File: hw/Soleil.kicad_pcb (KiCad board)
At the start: 2 copper layers, 31.4 x 44 mm, 41 parts, among them J1 Conn_01x04, Q1 Si2301, Q2 2N7002, SW1 SW_Push, U1 SPV1040TTR, U2 SPX3819M5-L-3-3, U3 STM32G030F6Px, U4 ZJY200200-0154DAAMFGN

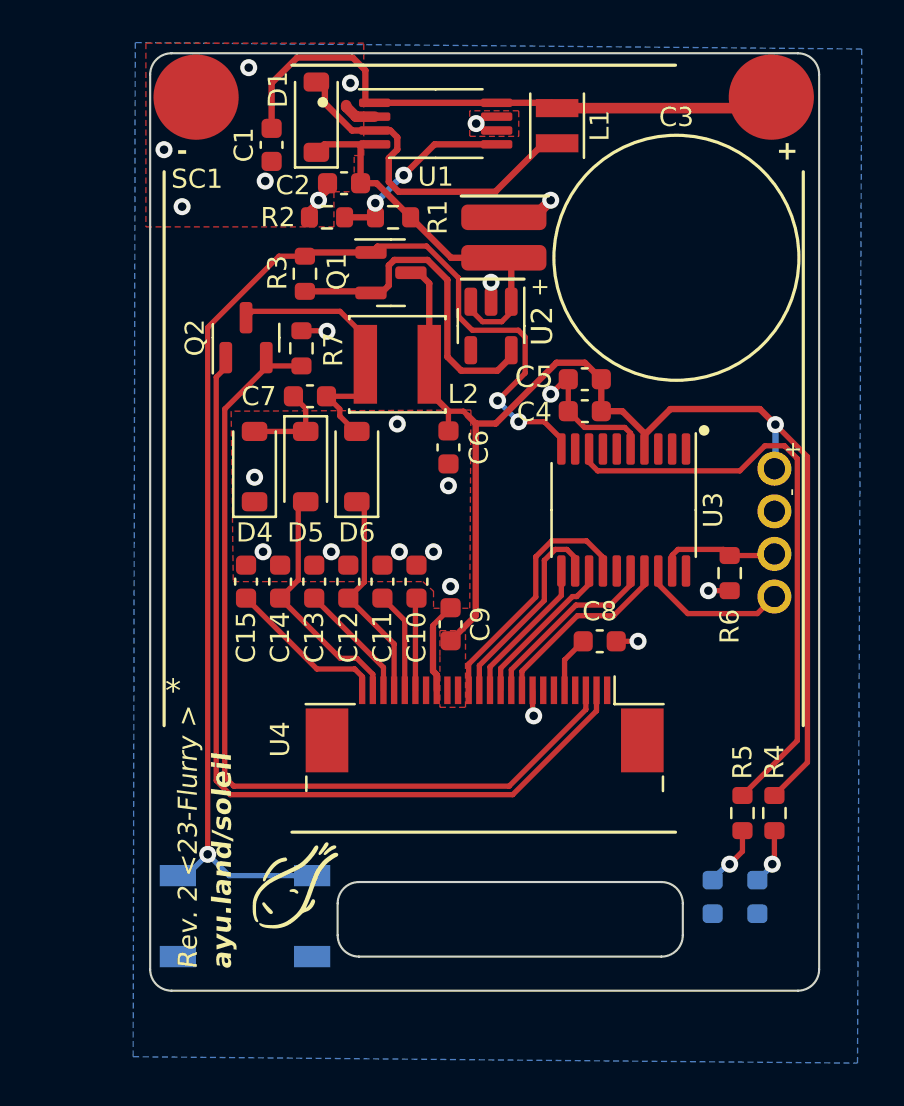
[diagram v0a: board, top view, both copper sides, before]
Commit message: (WIP) Update PCB layout, routing to-do
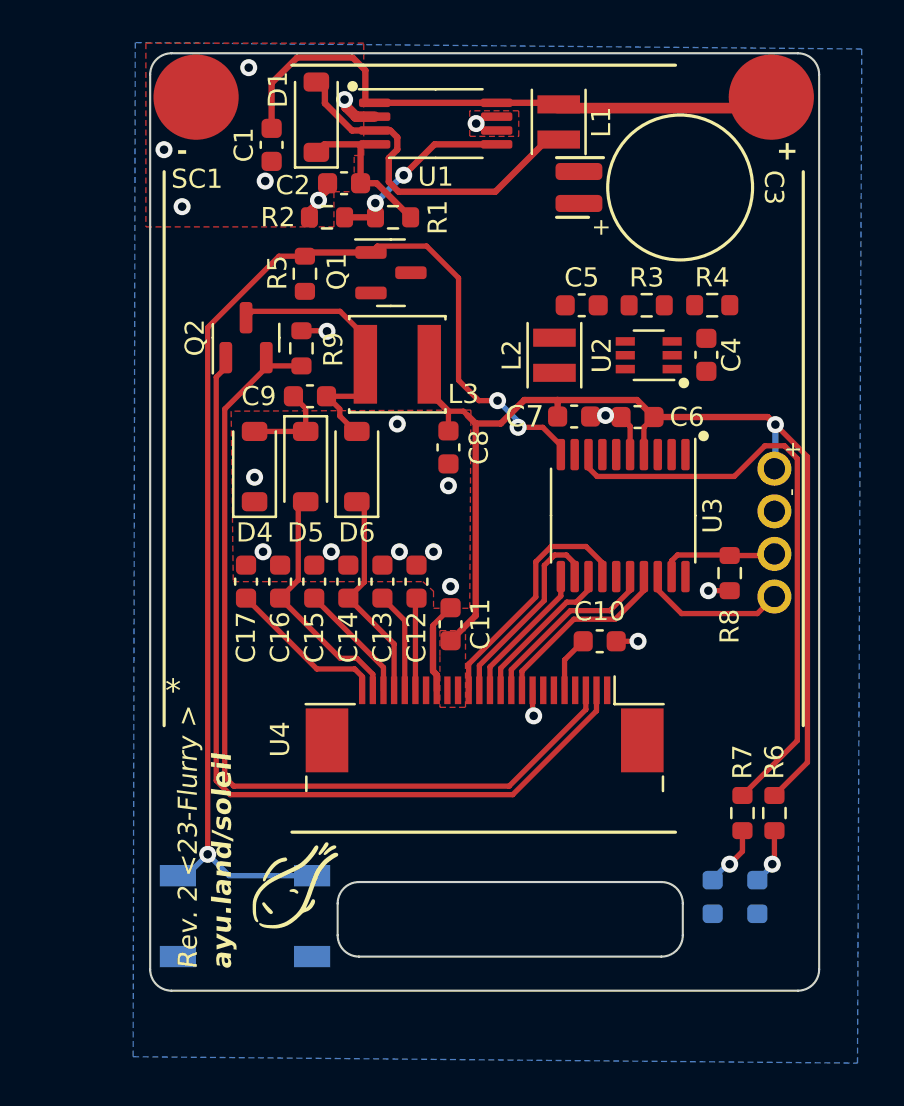
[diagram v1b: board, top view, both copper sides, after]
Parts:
- added C4: 10u, Capacitor_SMD:C_0603_1608Metric, F.Cu at (32.2, 23.6)
- added C5: 10u, Capacitor_SMD:C_0603_1608Metric, F.Cu at (26.4, 21.2)
- added L2: 10u, Inductor_SMD:L_Sunlord_SWPA252012S, F.Cu at (25.1, 23.6)
- added R3: 560k, Resistor_SMD:R_0603_1608Metric, F.Cu at (29.4, 21.2)
- added R4: 100k, Resistor_SMD:R_0603_1608Metric, F.Cu at (32.5, 21.2)
- C3: value 470m -> 220m; footprint Soleil_footprints:SuperCap_D11.5 -> Soleil_footprints:DMS3R3
- R1: value 750k -> 360k
- R7: renamed from R5; value 1k -> 820
- U2: value SPX3819M5-L-3-3 -> TPS61220DCK; footprint Package_TO_SOT_SMD:SOT-23-5 -> Package_TO_SOT_SMD:Texas_R-PDSO-G6
- moved U2 7.53 mm to (29.5, 23.6), turned to 180 degrees
- moved C3 3.30 mm to (31.0, 15.7)
- moved C6 2.49 mm to (29.0, 26.5)
- moved C7 1.82 mm to (26.0, 26.4), turned to 180 degrees
- moved U3 0.26 mm to (28.3, 31.1)
- moved L1 0.19 mm to (25.3, 12.6)
- renumbered C8 to C10, C9 to C11, C10 to C12, C11 to C13, C12 to C14, C13 to C15, C14 to C16, C15 to C17, C4 to C6, C5 to C7, C6 to C8, C7 to C9, L2 to L3, R3 to R5, R4 to R6, R6 to R8, R7 to R9
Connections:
- C2 pad 1: Net-(D1-K) -> VCAP
- C3 pad 1: Net-(D1-K) -> VCAP
- D1 pad 1: Net-(D1-K) -> VCAP
- Q1 pad 2: VREF -> VCAP
- Q1 pad 3: VDD -> VREF
- R1 pad 1: Net-(D1-K) -> VCAP
- R5 pad 1: VREF -> VCAP
- U1 pad 4: Net-(D1-K) -> VCAP
- U2 pad 1: Net-(D1-K) -> VREF
- U2 pad 2: GND -> Net-(U2-FB)
- U2 pad 3: Net-(D1-K) -> GND
- U2 pad 4: unconnected-(U2-BP-Pad4) -> VDD
- U2 pad 5: VREF -> Net-(U2-L)
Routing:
- net Net-(D1-K): track 18.3 -> 0.00 mm
- net VREF: track 15.8 -> 0.00 mm
- net VCAP: track 0.00 -> 7.71 mm
- net GND: track 20.8 -> 14.3 mm, vias 22 -> 20
- net VDD: track 61.0 -> 54.9 mm
- net PWR_LATCH: track 58.9 -> 57.1 mm

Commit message: Finish routing for the updated board
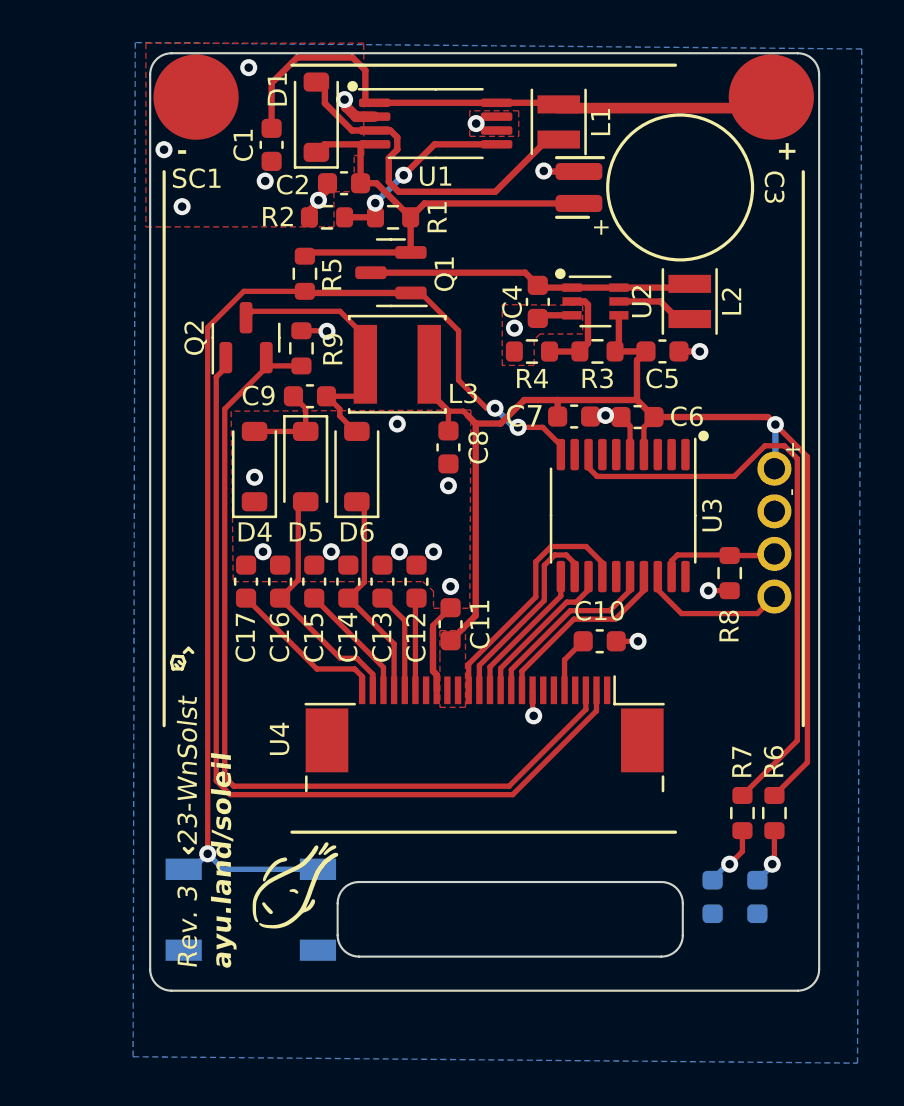
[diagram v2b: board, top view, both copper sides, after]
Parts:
- moved R4 8.74 mm to (24.0, 23.4), turned to 180 degrees
- moved C4 8.29 mm to (24.3, 21.1), turned to -90 degrees
- moved L2 6.83 mm to (31.4, 21.1), turned to -90 degrees
- moved C5 4.36 mm to (30.1, 23.4), turned to 0 degrees
- moved U2 3.55 mm to (27.0, 21.1), turned to 0 degrees
- moved R3 3.17 mm to (27.1, 23.4), turned to 180 degrees
- moved SW1 0.41 mm to (10.8, 49.6)
- turned Q1 to 180 degrees
- turned R5 to -90 degrees
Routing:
- net VREF: track 0.00 -> 15.3 mm
- net VCAP: track 7.71 -> 22.6 mm
- net VDD: track 54.9 -> 60.5 mm
- net Net-(U2-FB): track 0.00 -> 4.59 mm
- net GND: track 14.3 -> 18.6 mm, vias 20 -> 23
- net Net-(U2-L): track 0.00 -> 3.67 mm
- net PWR_LATCH: track 57.1 -> 53.7 mm
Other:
- board text added: "23-WnSolst"
- board text added: "Rev. 3"
- board text removed: "*"
- board text removed: "Rev. 2 <23-Flurry >"

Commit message: Add capacitor voltage sensing
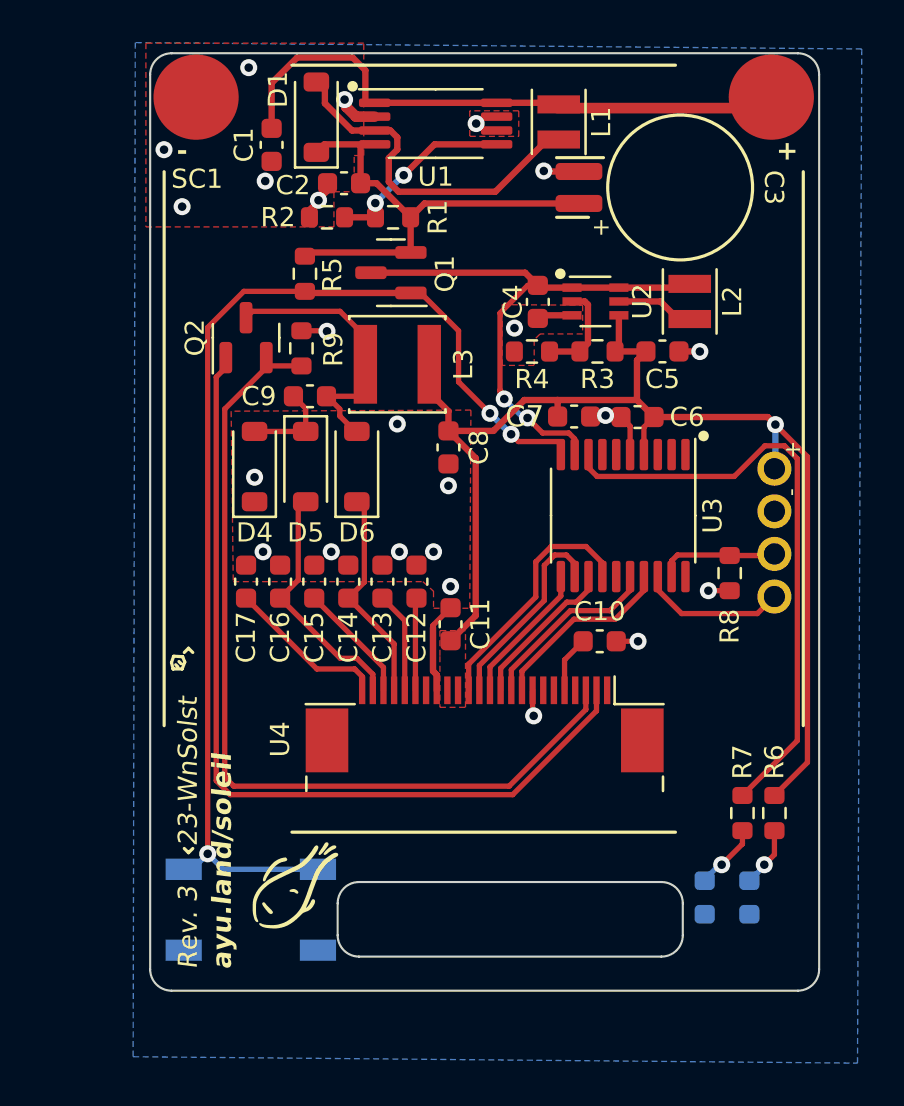
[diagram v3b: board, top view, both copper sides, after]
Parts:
- moved D2 0.38 mm to (34.2, 49.0)
- moved D3 0.38 mm to (32.1, 49.0)
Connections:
- U3 pad 9: unconnected-(U3-PA2-Pad9) -> VREF
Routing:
- net VREF: track 15.3 -> 27.0 mm, vias 0 -> 2

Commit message: Change LED to SMD RGB; submit for fabrication
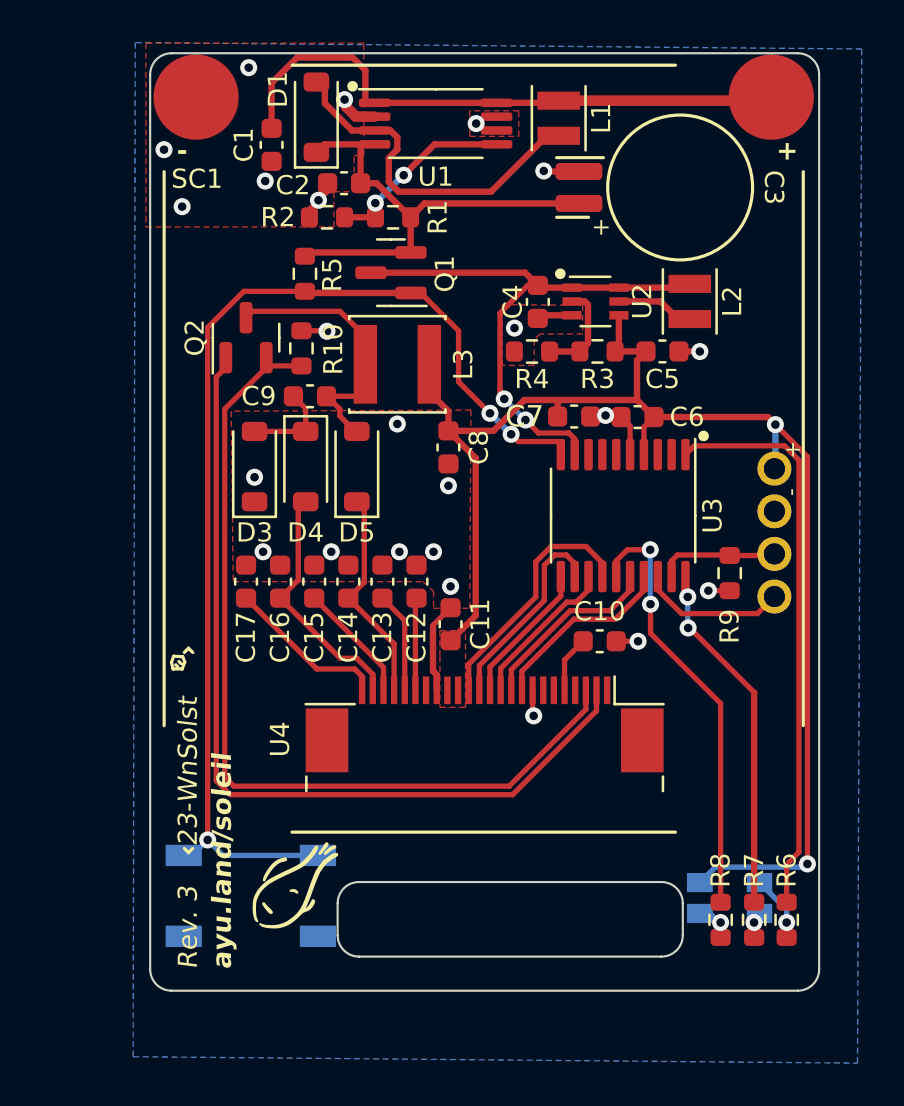
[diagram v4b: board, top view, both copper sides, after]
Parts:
- removed the D3 at (32.1, 49.0)
- added R8: TBD, Resistor_SMD:R_0603_1608Metric, F.Cu at (32.9, 50.1)
- D2: value White -> LED_RABG; footprint LED_SMD:LED_0603_1608Metric -> LED_SMD:LED_Kingbright_AAA3528ESGCT
- R6: value 2.7k -> TBD
- R7: value 820 -> TBD
- moved R6 5.05 mm to (36.0, 50.1), turned to 90 degrees
- moved R7 5.04 mm to (34.5, 50.1), turned to 90 degrees
- moved D2 0.93 mm to (33.3, 49.0), turned to 180 degrees
- moved SW1 0.65 mm to (10.8, 49.0)
- moved L1 0.18 mm to (25.3, 12.4)
- renumbered D4 to D3, D5 to D4, D6 to D5, R9 to R10, R8 to R9
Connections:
- D2 pad 1: GND -> Net-(D2-RK)
- D2 pad 2: Net-(D2-A) -> VDD
- R6 pad 1: VDD -> Net-(D2-RK)
- R6 pad 2: Net-(D2-A) -> LED_R
- R7 pad 1: ACT_LED -> Net-(D2-GK)
- R7 pad 2: Net-(D3-A) (its old number) -> LED_G
- U3 pad 1: unconnected-(U3-PB7/PB8-Pad1) -> LED_R
- U3 pad 15: unconnected-(U3-PB0/PB1/PB2/PA8-Pad15) -> LED_B
- U3 pad 20: unconnected-(U3-PB3/PB4/PB5/PB6-Pad20) -> LED_G
- U3 pad 8: ACT_LED -> unconnected-(U3-PA1-Pad8)
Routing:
- net ACT_LED: track 28.3 -> 0.00 mm
- net LED_R: track 0.00 -> 26.8 mm
- net LED_B: track 0.00 -> 20.4 mm, vias 0 -> 2
- net LED_G: track 0.00 -> 16.6 mm, vias 0 -> 2
- net VDD: track 60.6 -> 68.6 mm, vias 1 -> 2
- net Net-(D2-RK): track 0.00 -> 3.10 mm, vias 0 -> 1
- net Net-(D3-A) (its old number): track 3.09 -> 0.00 mm, vias 1 -> 0
- net Net-(D2-A): track 2.71 -> 0.00 mm, vias 1 -> 0
- net Net-(D2-BK): track 0.00 -> 1.85 mm, vias 0 -> 1
- net Net-(D2-GK): track 0.00 -> 0.70 mm, vias 0 -> 1
- net PWR_LATCH: track 53.7 -> 53.1 mm
- net unconnected-(U3-PA1-Pad8): track 0.00 -> 0.62 mm

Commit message: Revise circuit board design; submit for fab
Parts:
- removed the Q1 at (17.4, 19.7)
- D2: value LED_RABG -> LED_RGB; footprint LED_SMD:LED_Kingbright_AAA3528ESGCT -> Soleil_footprints:LED_BRG_KA_5050-6
- moved R6 6.53 mm to (36.0, 43.5)
- moved R7 6.53 mm to (34.5, 43.5)
- moved R8 6.53 mm to (32.9, 43.5)
- moved R3 3.97 mm to (23.2, 22.6), turned to 90 degrees
- moved R5 3.71 mm to (16.9, 20.8), turned to 180 degrees
- moved C4 3.11 mm to (27.1, 19.8), turned to 180 degrees
- moved C5 3.02 mm to (27.2, 24.1), turned to 180 degrees
- moved L2 1.24 mm to (30.2, 20.9)
- moved R4 1.01 mm to (24.7, 22.6), turned to -90 degrees
- moved U2 0.88 mm to (27.0, 21.9)
- moved D2 0.66 mm to (34.0, 49.0), turned to -90 degrees
- moved C3 0.20 mm to (31.0, 15.5)
- moved J1 0.15 mm to (35.5, 31.9)
- renumbered Q2 to Q1
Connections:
- net PWR_LATCH renamed BTN_INTR
- C4 pad 1: VREF -> VCAP
- D2 pad 1: Net-(D2-RK) -> GND
- D2 pad 2: VDD -> Net-(D2-BA)
- D2 pad 3: Net-(D2-BK) -> GND
- L2 pad 1: VREF -> VCAP
- R5 pad 1: VCAP -> VDD
- R6 pad 1: Net-(D2-RK) -> Net-(D2-GA)
- R6 pad 2: LED_R -> LED_G
- R7 pad 2: LED_G -> LED_R
- R8 pad 1: Net-(D2-BK) -> Net-(D2-BA)
- U2 pad 1: VREF -> VCAP
- U2 pad 6: VREF -> VCAP
- U3 pad 1: LED_R -> LED_G
- U3 pad 20: LED_G -> LED_R
- U3 pad 9: VREF -> VCAP
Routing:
- net VREF: track 27.0 -> 0.00 mm, vias 2 -> 0
- net VDD: track 68.6 -> 46.7 mm
- net LED_R: track 26.8 -> 10.1 mm, vias 0 -> 2
- net VCAP: track 22.6 -> 34.5 mm, vias 0 -> 2
- net LED_B: track 20.4 -> 13.9 mm
- net LED_G: track 16.6 -> 20.7 mm, vias 2 -> 0
- net Net-(U2-L): track 3.67 -> 0.00 mm
- net Net-(D2-RK): track 3.10 -> 0.00 mm, vias 1 -> 0
- net Net-(D2-BA): track 0.00 -> 2.56 mm, vias 0 -> 1
- net Net-(D2-GA): track 0.00 -> 2.39 mm, vias 0 -> 1
- net Net-(D2-BK): track 1.85 -> 0.00 mm, vias 1 -> 0
- net Net-(U2-FB): track 4.59 -> 2.78 mm
- net Net-(D2-RA): track 0.70 -> 2.38 mm
- net GND: track 18.6 -> 17.9 mm, vias 23 -> 27
- net BTN_INTR: vias 3 -> 1
- added copper zone on F.Cu, net Net-(U2-L)
- added copper zone on F.Cu, net VCAP
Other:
- board text added: "24-Bedew"
- board text added: "Le Petit soleil Lenormand"
- board text added: "Rev. 4"
- board text removed: "23-WnSolst"
- board text removed: "Le petit soleil Lenormand"
- board text removed: "Rev. 3"

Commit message: Revise board design; submit for fab (Rev. 5)
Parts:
- removed the D1 at (13.9, 12.4)
- added C19: 100n, Capacitor_SMD:C_0603_1608Metric, F.Cu at (22.3, 30.1)
- added C4: 100n, Capacitor_SMD:C_0603_1608Metric, F.Cu at (19.0, 19.3)
- added Q1: MMBT3904, Package_TO_SOT_SMD:SOT-23, F.Cu at (16.3, 17.8)
- added R3: 470k, Resistor_SMD:R_0603_1608Metric, F.Cu at (19.6, 16.9)
- added R4: 470k, Resistor_SMD:R_0603_1608Metric, F.Cu at (13.8, 18.3)
- added U2: XS3A1T3157GMX, Soleil_footprints:XS3A1T3157GMX, F.Cu at (20.6, 18.8)
- added U6: W25Q16JVUXIQ, Soleil_footprints:SON50P300X200X60-9N, F.Cu at (24.4, 30.8)
- R10: renamed from R6; value TBD -> 4.7k
- R11: renamed from R8; value TBD -> 4.7k
- R9: renamed from R7; value TBD -> 4.7k
- moved C1 12.8 mm to (24.4, 11.5)
- moved L1 11.0 mm to (14.3, 11.7)
- moved R2 6.04 mm to (19.8, 14.4)
- moved R1 5.97 mm to (22.8, 14.4)
- moved R5 5.66 mm to (22.1, 18.4), turned to 90 degrees
- moved C2 1.94 mm to (16.8, 14.4)
- moved C8 1.10 mm to (27.1, 26.5)
- moved C7 1.10 mm to (30.1, 26.5)
- moved U4 1.10 mm to (29.4, 31.1)
- moved U1 0.81 mm to (19.6, 11.9)
- moved C3 0.54 mm to (30.9, 15.0)
- moved R8 0.53 mm to (33.8, 33.8)
- moved C11 0.45 mm to (27.5, 37.4)
- moved D1 0.20 mm to (34.0, 49.1)
- moved SW1 0.20 mm to (10.8, 49.1)
- renumbered C9 to C10, C10 to C11, C11 to C12, C12 to C13, C13 to C14, C14 to C15, C15 to C16, C16 to C17, C17 to C18, C4 to C5, C5 to C6, C6 to C7, C7 to C8, C8 to C9, D2 to D1, D3 to D2, D4 to D3, D5 to D4, Q1 to Q2, R10 to R12, R3 to R6, R4 to R7, R9 to R8, U2 to U3, U3 to U4, U4 to U5
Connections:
- net EP_MOSI renamed SPI_MOSI
- net EP_NCS renamed EP_CSN
- net EP_SCK renamed SPI_SCK
- C5 pad 1: VCAP -> VRI
- L2 pad 1: VCAP -> VRI
- R5 pad 1: VDD -> VCAP
- R5 pad 2: BTN_INTR -> PWR_LATCH
- SW1 pad 1: BTN_INTR -> VCAP
- SW1 pad 2: GND -> Net-(U2-Y2)
- U3 pad 1: VCAP -> VRI
- U3 pad 6: VCAP -> VRI
- U4 pad 10: BTN_INTR -> PWR_LATCH
- U4 pad 13: EP_DCC -> SPI_MISO
- U4 pad 2: unconnected-(U3-PC14/PB9-Pad2) -> FLASH_CSN
- U4 pad 7: unconnected-(U3-PA0-Pad7) -> VCAP
- U4 pad 8: unconnected-(U3-PA1-Pad8) -> EP_DCC
- U4 pad 9: VCAP -> BTN_INTR
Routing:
- net Net-(U2-Y2): track 0.00 -> 53.7 mm, vias 0 -> 1
- net VCAP: track 34.5 -> 79.6 mm, vias 2 -> 3
- net BTN_INTR: track 53.1 -> 20.5 mm, vias 1 -> 2
- net VRI: track 0.00 -> 16.4 mm, vias 0 -> 2
- net PWR_LATCH: track 0.00 -> 15.5 mm, vias 0 -> 2
- net Net-(U1-LX): track 16.8 -> 2.58 mm
- net EP_DCC: track 7.30 -> 16.3 mm, vias 0 -> 2
- net VDD: track 46.7 -> 55.6 mm, vias 2 -> 4
- net FLASH_CSN: track 0.00 -> 7.99 mm, vias 0 -> 2
- net SPI_MISO: track 0.00 -> 6.47 mm, vias 0 -> 2
- net Net-(SC1-+): track 27.5 -> 21.7 mm
- net Net-(U1-VCTRL): track 8.96 -> 3.41 mm, vias 2 -> 0
- net GND: track 17.9 -> 21.4 mm, vias 27 -> 28
- net SPI_MOSI: track 11.7 -> 15.1 mm
- net SPI_SCK: track 9.54 -> 12.4 mm, vias 0 -> 2
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- added copper zone on F.Cu, net VRI
- removed copper zone on F.Cu, net VCAP
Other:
- board text added: "24-Arouse"
- board text added: "Rev. 5"
- board text removed: "24-Bedew"
- board text removed: "Rev. 4"
